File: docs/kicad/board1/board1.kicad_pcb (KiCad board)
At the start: 2 copper layers, 100.3 x 91.4 mm, 44 parts, among them J1 INST_POWER, J10 SN65HVD230, J11 CAN_TERMINATOR, J14 MAX3232, J15 AIS, J16 GPS, J17 ST_CONNECTED, J2 NMEA2000, J21 ST1, J22 ST1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

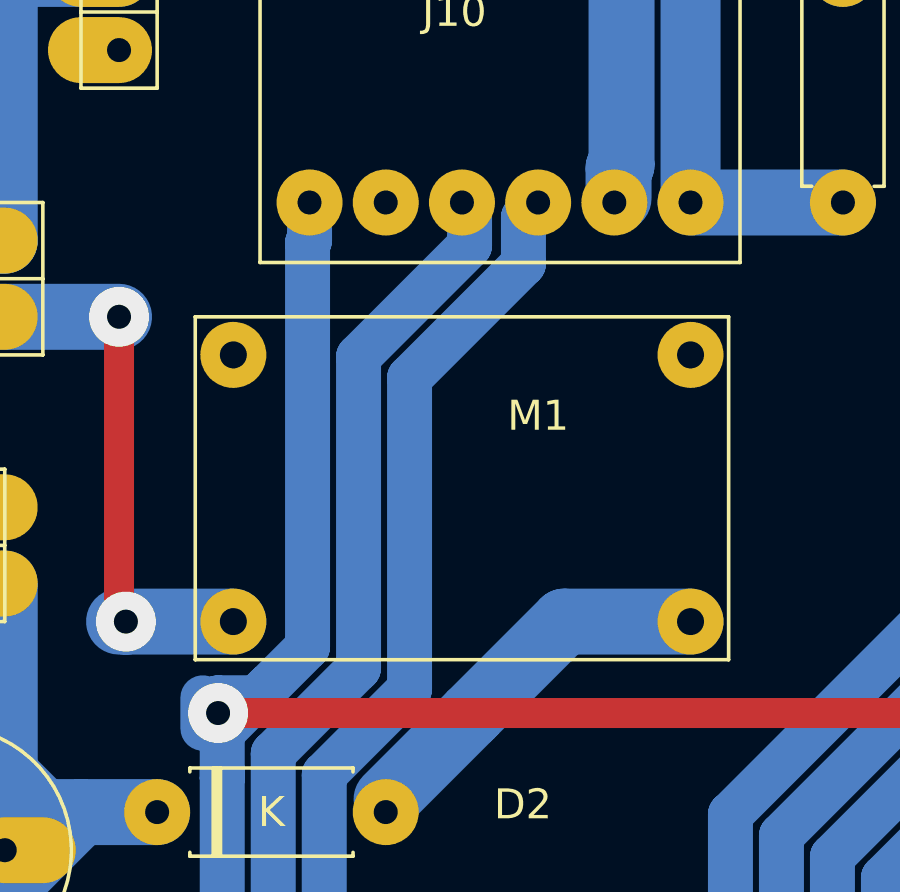
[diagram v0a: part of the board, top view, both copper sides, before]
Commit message: fix incorrect CRX/CTX routing
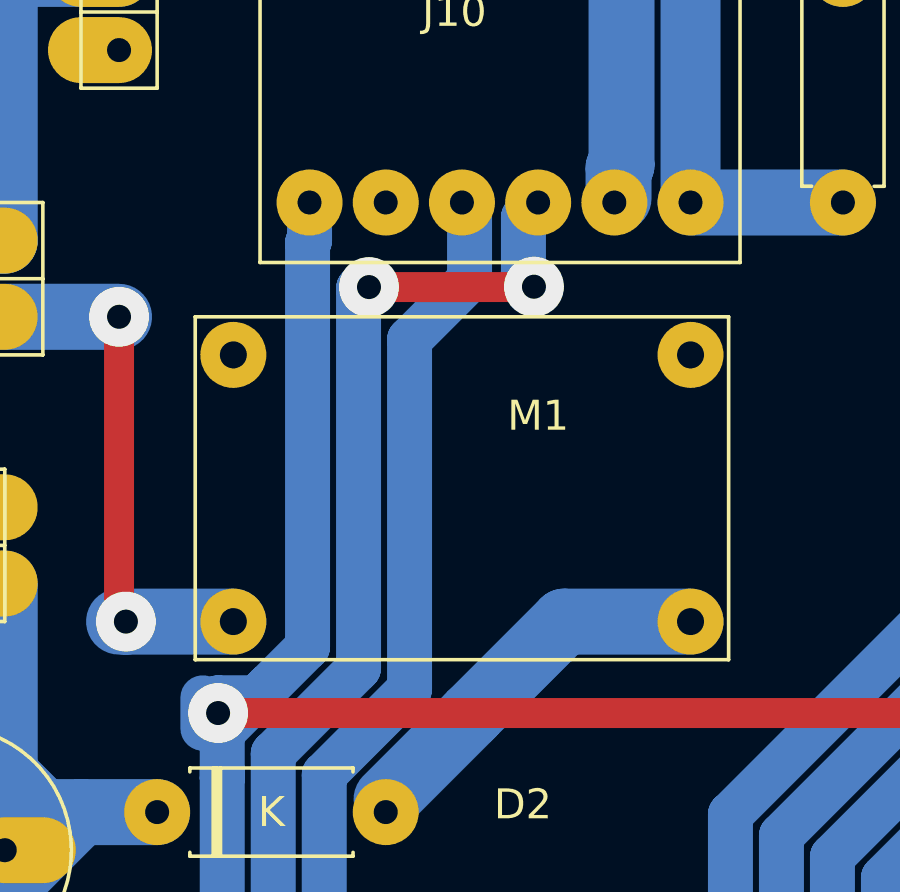
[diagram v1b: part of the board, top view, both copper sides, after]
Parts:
- R1: value 4.7K -> 10K
- R7: value 4.7K -> 10k
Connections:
- U3 pad 24: CRX -> CTX
- U3 pad 25: CTX -> CRX
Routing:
- net CRX: track 34.4 -> 39.6 mm, vias 0 -> 2
- net CTX: track 35.0 -> 33.5 mm
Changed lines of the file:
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@@
     (thickness 1.6)
     (drawings 5)
-    (tracks 455)
+    (tracks 462)
     (zones 0)
     (modules 44)
@@
       (net 21 RX5))
     (pad 24 thru_hole oval (at 10.16 -15.24) (size 2.2 3.47) (drill 0.8 (offset 0 -0.635)) (layers *.Cu *.Mask)
+      (net 24 CTX))
+    (pad 25 thru_hole oval (at 7.62 -15.24) (size 2.2 3.47) (drill 0.8 (offset 0 -0.635)) (layers *.Cu *.Mask)
       (net 25 CRX))
-    (pad 25 thru_hole oval (at 7.62 -15.24) (size 2.2 3.47) (drill 0.8 (offset 0 -0.635)) (layers *.Cu *.Mask)
-      (net 24 CTX))
     (pad 26 thru_hole oval (at 5.08 -15.24) (size 2.2 3.47) (drill 0.8 (offset 0 -0.635)) (layers *.Cu *.Mask)
       (net 23 +3V3))
@@
       (effects (font (size 1 1) (thickness 0.15)))
     )
-    (fp_text value 4.7K (at 3.8608 2.5654 90) (layer F.Fab)
+    (fp_text value 10K (at 4.064 0 90) (layer F.Fab)
       (effects (font (size 1 1) (thickness 0.15)))
     )
@@
       (effects (font (size 1 1) (thickness 0.15)))
     )
-    (fp_text value 220 (at 3.7846 2.5146 90) (layer F.Fab)
+    (fp_text value 220 (at 3.556 0 90) (layer F.Fab)
       (effects (font (size 1 1) (thickness 0.15)))
     )
@@
       (effects (font (size 1 1) (thickness 0.15)))
     )
-    (fp_text value 4.7K (at 3.81 2.54 90) (layer F.Fab)
+    (fp_text value 10k (at 4.064 0 90) (layer F.Fab)
       (effects (font (size 1 1) (thickness 0.15)))
     )
@@
       (effects (font (size 1 1) (thickness 0.15)))
     )
-    (fp_text value 220 (at 3.81 2.54 90) (layer F.Fab)
+    (fp_text value 220 (at 3.556 0 90) (layer F.Fab)
       (effects (font (size 1 1) (thickness 0.15)))
     )
@@
   (segment (start 34.15001 105.309991) (end 34.050001 105.41) (width 1) (layer F.Cu) (net 23))
   (segment (start 34.15001 90.17) (end 34.15001 105.309991) (width 1) (layer F.Cu) (net 23))
-  (segment (start 0.05998 87.06202) (end -1.27 88.392) (width 1.5) (layer B.Cu) (net 24))
-  (segment (start 0.05998 76.783843) (end 0.05998 87.06202) (width 1.5) (layer B.Cu) (net 24))
-  (segment (start -1.27 88.392) (end -1.27 90.17) (width 1.5) (layer B.Cu) (net 24))
-  (segment (start 2.903624 73.9402) (end 0.05998 76.783843) (width 1.5) (layer B.Cu) (net 24))
-  (segment (start 6.604 59.857457) (end 2.903624 63.557833) (width 1.5) (layer B.Cu) (net 24))
-  (segment (start 2.903624 63.557833) (end 2.903624 73.9402) (width 1.5) (layer B.Cu) (net 24))
-  (segment (start 6.604 58.42) (end 6.604 59.857457) (width 1.5) (layer B.Cu) (net 24))
-  (segment (start 1.75999 86.780859) (end 1.75999 89.916) (width 1.5) (layer B.Cu) (net 25))
-  (segment (start 1.75999 77.48801) (end 1.75999 86.780859) (width 1.5) (layer B.Cu) (net 25))
-  (segment (start 8.89 58.42) (end 8.400001 58.909999) (width 1.5) (layer B.Cu) (net 25))
-  (segment (start 8.400001 58.909999) (end 8.400001 60.465633) (width 1.5) (layer B.Cu) (net 25))
-  (segment (start 8.400001 60.465633) (end 4.603634 64.262) (width 1.5) (layer B.Cu) (net 25))
-  (segment (start 4.603634 64.262) (end 4.603634 74.644366) (width 1.5) (layer B.Cu) (net 25))
-  (segment (start 4.603634 74.644366) (end 1.75999 77.48801) (width 1.5) (layer B.Cu) (net 25))
+  (segment (start 1.75999 86.780859) (end 1.75999 89.916) (width 1.5) (layer B.Cu) (net 24))
+  (segment (start 6.604 58.42) (end 6.604 60.9854) (width 1.5) (layer B.Cu) (net 24))
+  (segment (start 6.604 60.9854) (end 4.603634 62.985766) (width 1.5) (layer B.Cu) (net 24))
+  (segment (start 4.603634 62.985766) (end 4.603634 74.644366) (width 1.5) (layer B.Cu) (net 24))
+  (segment (start 4.603634 74.644366) (end 1.75999 77.48801) (width 1.5) (layer B.Cu) (net 24))
+  (segment (start 1.75999 77.48801) (end 1.75999 86.780859) (width 1.5) (layer B.Cu) (net 24))
+  (segment (start 8.400001 58.909999) (end 8.89 58.42) (width 1.5) (layer B.Cu) (net 25))
+  (segment (start 8.400001 60.724001) (end 8.400001 58.909999) (width 1.5) (layer B.Cu) (net 25))
+  (segment (start 8.400001 60.724001) (end 8.400001 60.876401) (width 1.5) (layer B.Cu) (net 25))
+  (segment (start 8.400001 60.876401) (end 8.7503 61.2267) (width 1.5) (layer B.Cu) (net 25))
+  (via (at 8.7503 61.2267) (size 2) (drill 0.8) (layers F.Cu B.Cu) (net 25))
+  (via (at 3.2512 61.2394) (size 2) (drill 0.8) (layers F.Cu B.Cu) (net 25))
+  (segment (start -1.27 88.392) (end -1.27 90.17) (width 1.5) (layer B.Cu) (net 25))
+  (segment (start 0.05998 87.06202) (end -1.27 88.392) (width 1.5) (layer B.Cu) (net 25))
+  (segment (start 2.9464 61.2394) (end 2.903624 61.282176) (width 1.5) (layer B.Cu) (net 25))
+  (segment (start 3.2512 61.2394) (end 2.9464 61.2394) (width 1.5) (layer B.Cu) (net 25))
+  (segment (start 2.903624 61.282176) (end 2.903624 73.9402) (width 1.5) (layer B.Cu) (net 25))
+  (segment (start 2.903624 73.9402) (end 0.05998 76.783843) (width 1.5) (layer B.Cu) (net 25))
+  (segment (start 0.05998 76.783843) (end 0.05998 87.06202) (width 1.5) (layer B.Cu) (net 25))
+  (segment (start 8.7376 61.2394) (end 8.7503 61.2267) (width 1) (layer F.Cu) (net 25))
+  (segment (start 3.2512 61.2394) (end 8.7376 61.2394) (width 1) (layer F.Cu) (net 25))
   (segment (start 16.51 90.17) (end 16.51 88.540849) (width 1.5) (layer B.Cu) (net 26))
   (segment (start 16.713525 88.2015) (end 16.357763 88.557262) (width 1.5) (layer B.Cu) (net 26))

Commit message: renamed 8 pin connector net names in accordance with comments
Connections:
- net Net-(U3-Pad6) renamed UDP_ENABLE
- net POT_CS1 renamed SDA-WIND_PULSE-LCD_DC
- net POT_CS2 renamed SCL-GP-T_CS
- net POT_MISO renamed MISO-GP
- net POT_SCLK renamed SCLK-GP
- net SPEED_PULSE renamed SPEED_PULSE-LCD_CS
- net WIND_PULSE renamed MOSI-GP
- U3 pad 24: CTX -> CRX
- U3 pad 25: CRX -> CTX

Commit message: reworked existing teensyBoat PCB for tbESP32 connector - ran Serial5 (RX5 & TX5) to 8 pin connector - updated schematic and PCB with comments - changed PIN_UDP_ENABLE from 4 to 12 (mosi)
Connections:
- net MISO-GP renamed MISO-UDP_ENABLE
- J6 pad 1: SCL-GP-T_CS -> TX5-LCD_DC
- J6 pad 2: SDA-WIND_PULSE-LCD_DC -> RX5-T_CS
- U3 pad 20: SDA-WIND_PULSE-LCD_DC -> Net-(U3-Pad20)
- U3 pad 21: SCL-GP-T_CS -> Net-(U3-Pad21)
- U3 pad 22: TX5 -> TX5-LCD_DC
- U3 pad 23: RX5 -> RX5-T_CS
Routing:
- net RX5-T_CS: track 0.00 -> 80.6 mm, vias 0 -> 4
- net TX5-LCD_DC: track 0.00 -> 77.7 mm, vias 0 -> 4
- net SDA-WIND_PULSE-LCD_DC: track 76.1 -> 0.00 mm, vias 4 -> 0
- net SCL-GP-T_CS: track 74.3 -> 0.00 mm, vias 4 -> 0
- net Net-(U3-Pad20): track 0.00 -> 7.98 mm
- net TX5: track 4.17 -> 0.00 mm, vias 1 -> 0
- net Net-(U3-Pad21): track 0.00 -> 3.81 mm
- net RX5: track 2.54 -> 0.00 mm, vias 1 -> 0
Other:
- board text added: "Note that RX5 connected to TEST_RIG via "just in case" pads from initial design, which should be reworked if another teensyBoat PCB is created."

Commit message: created 2nd teensyBoat PCB then modified Pheonix connector pads and deleted plot/gcode
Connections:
- J10 pad 3: CTX -> CRX
- J10 pad 4: CRX -> CTX
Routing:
- net CTX: track 33.5 -> 39.6 mm, vias 0 -> 2
- net CRX: track 39.6 -> 33.5 mm, vias 2 -> 0
